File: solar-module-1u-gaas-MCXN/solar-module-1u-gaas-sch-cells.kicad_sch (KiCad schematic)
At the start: 3 parts

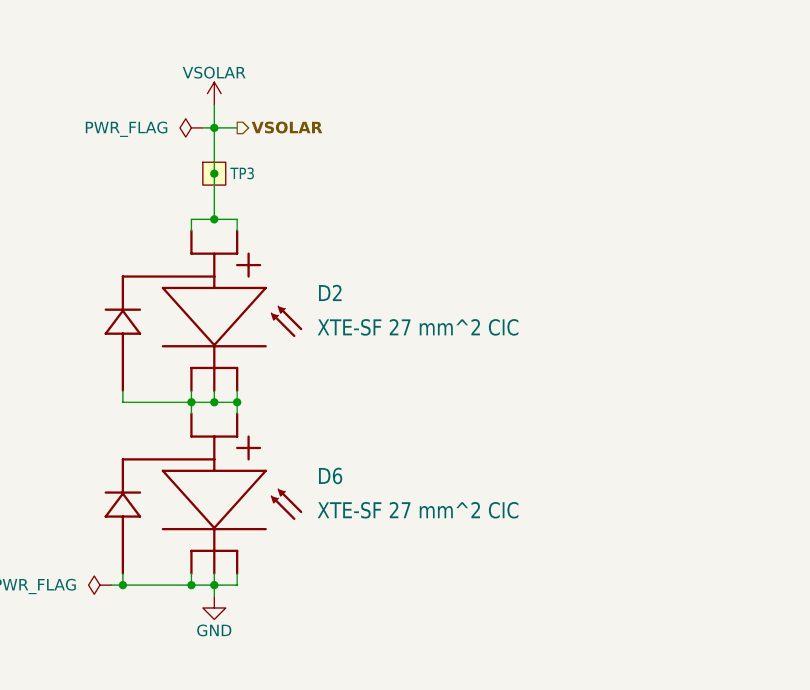
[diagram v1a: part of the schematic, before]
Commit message: Minor polishing to schematic and board: fixed value font sizes and placement, imported value fixes to layout.
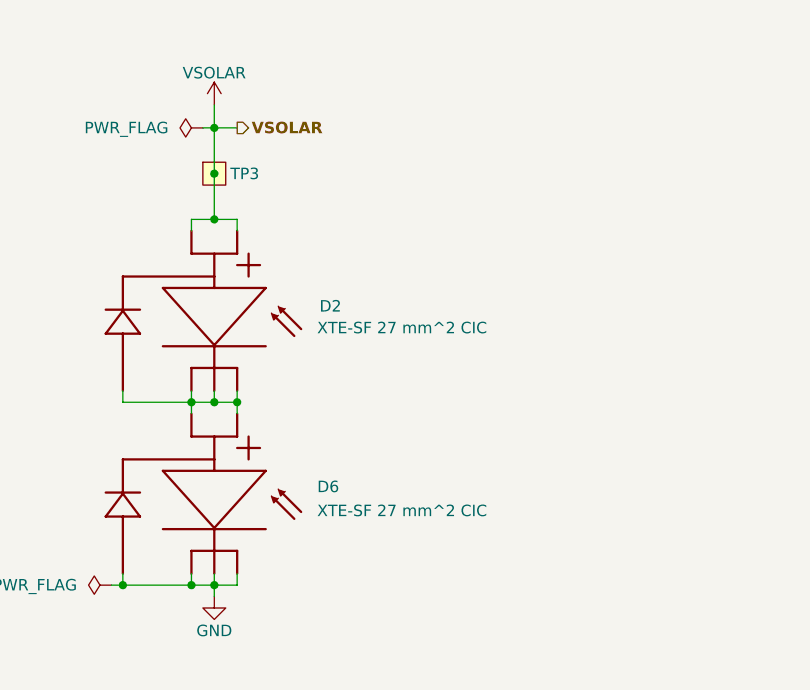
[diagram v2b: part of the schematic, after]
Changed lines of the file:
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@@
 		(in_pos_files yes)
 		(dnp no)
-		(fields_autoplaced yes)
 		(property "Reference" "D2"
-			(at 219.71 140.335 0)
-			(show_name no)
-			(do_not_autoplace no)
-			(effects
-				(font
-					(size 1.778 1.5113)
+			(at 219.964 141.732 0)
+			(show_name no)
+			(do_not_autoplace no)
+			(effects
+				(font
+					(size 1.27 1.27)
 				)
 				(justify left)
@@
 			(effects
 				(font
-					(size 1.778 1.5113)
+					(size 1.27 1.27)
 				)
 				(justify left)
@@
 		(in_pos_files yes)
 		(dnp no)
-		(fields_autoplaced yes)
 		(property "Reference" "D6"
-			(at 219.71 160.655 0)
-			(show_name no)
-			(do_not_autoplace no)
-			(effects
-				(font
-					(size 1.778 1.5113)
+			(at 219.71 161.798 0)
+			(show_name no)
+			(do_not_autoplace no)
+			(effects
+				(font
+					(size 1.27 1.27)
 				)
 				(justify left)
@@
 			(effects
 				(font
-					(size 1.778 1.5113)
+					(size 1.27 1.27)
 				)
 				(justify left)
@@
 			(effects
 				(font
-					(size 1.27 1.0795)
+					(size 1.27 1.27)
 				)
 				(justify left bottom)
